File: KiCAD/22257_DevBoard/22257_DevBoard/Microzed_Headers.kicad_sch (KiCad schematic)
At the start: 11 parts, among them J1 TD-120-G-AACON40_2X20_TU_HTS_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, J2 TD-120-G-AACON40_2X20_TU_HTS_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

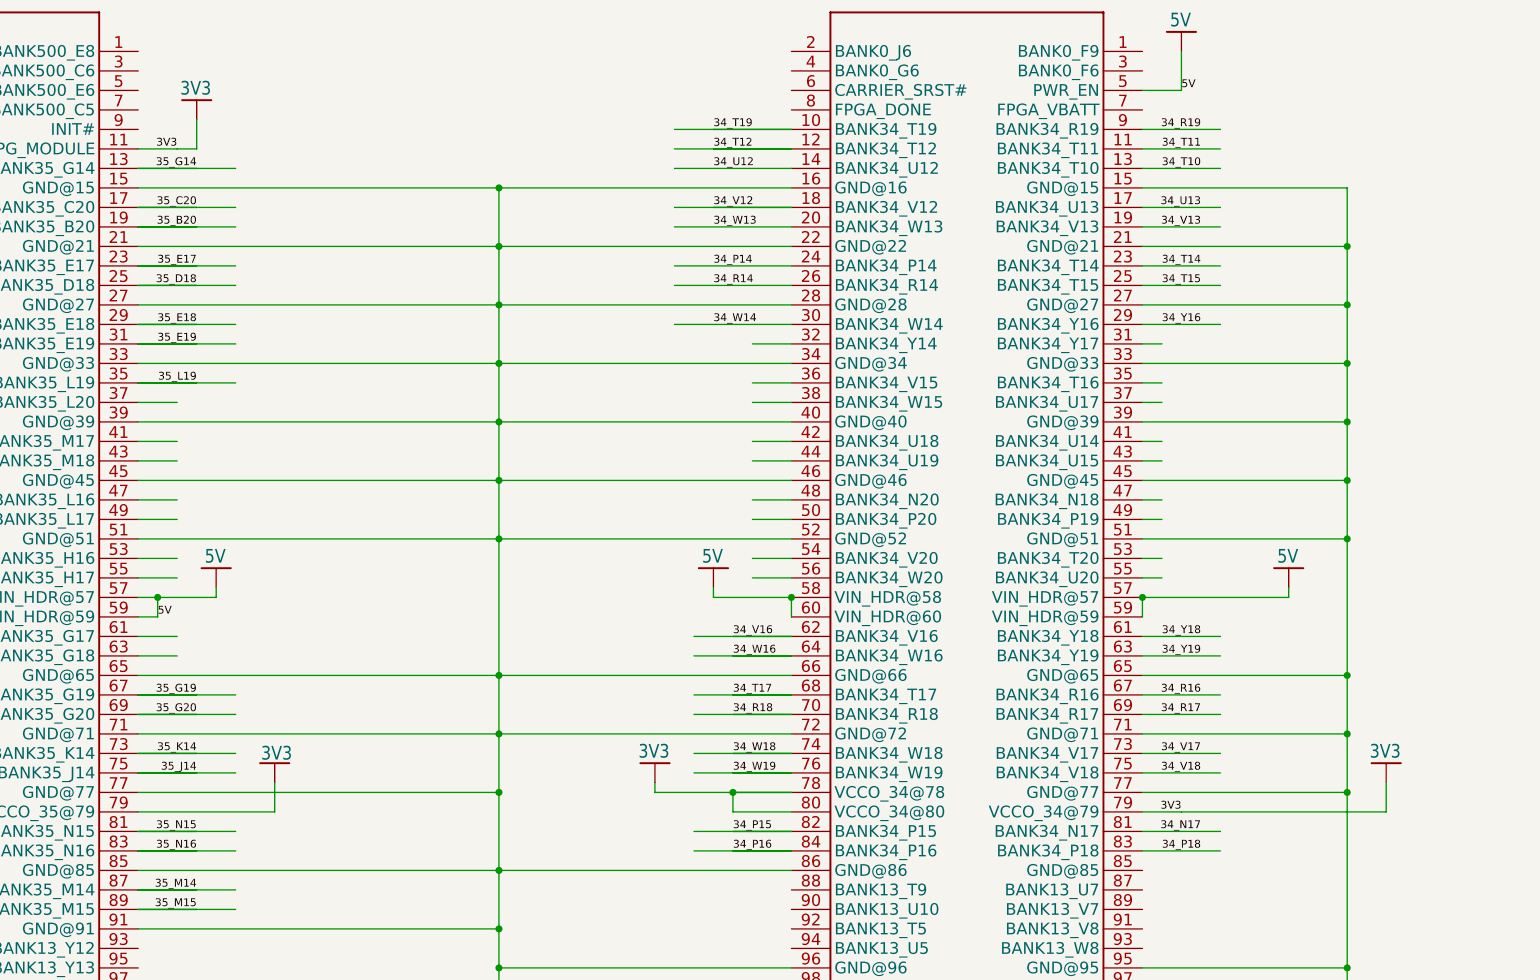
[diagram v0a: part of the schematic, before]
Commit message: Schematic Progress. Added connections to the MicroZed and added a 3v3 rail regulator
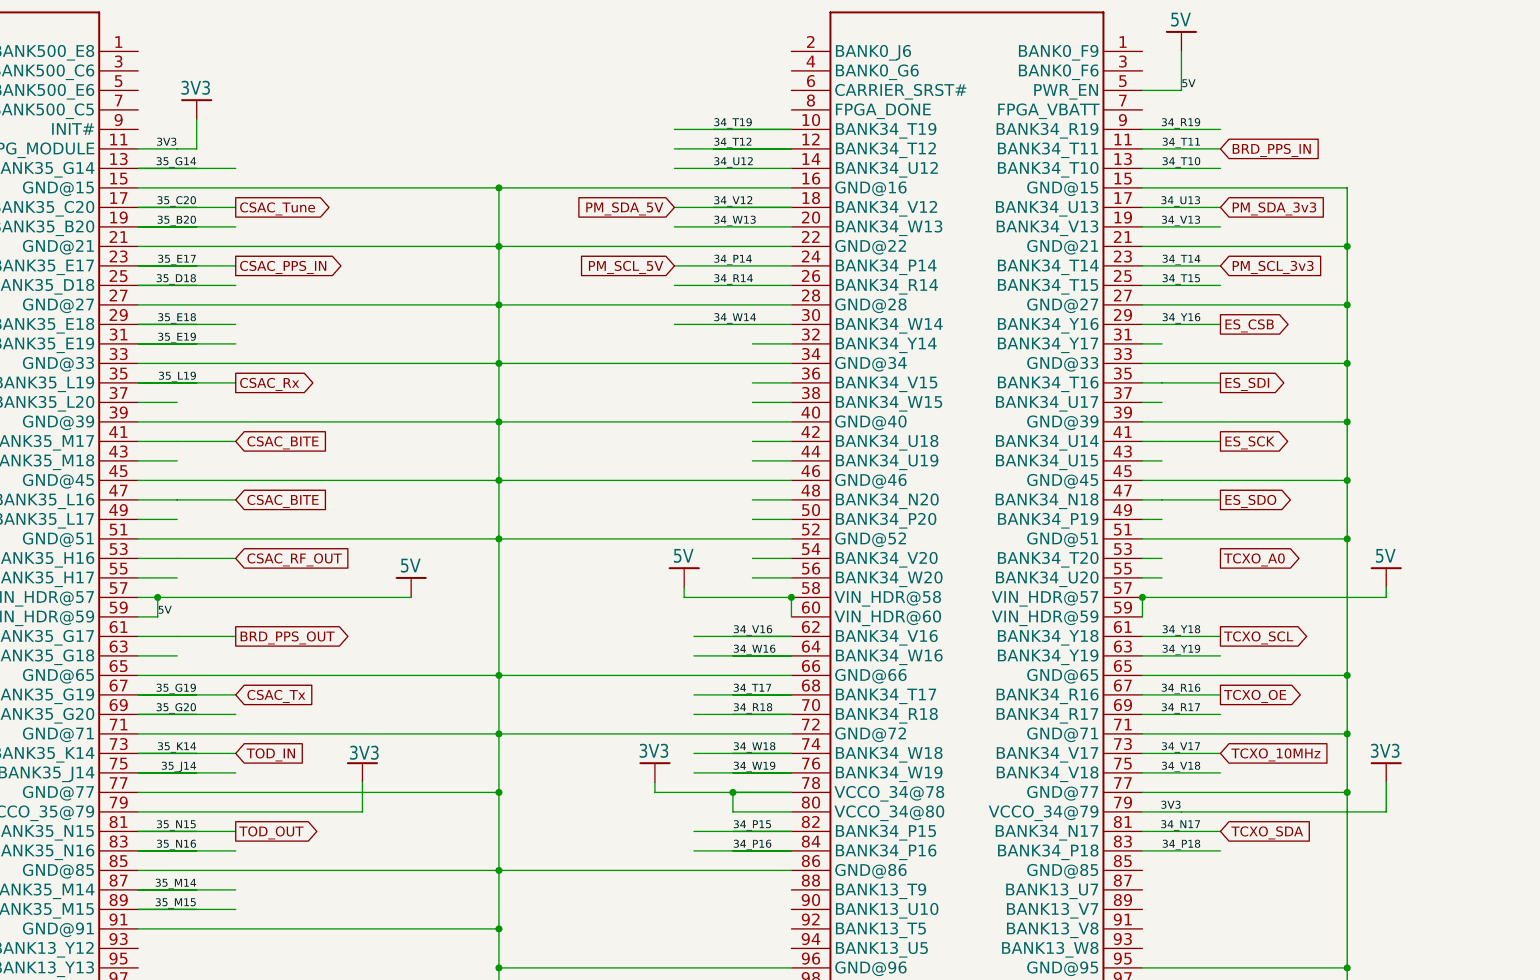
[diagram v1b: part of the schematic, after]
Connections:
- net ES_SDI: now reaches JX2.35 (BANK34_T16)
- net ES_SCK: now reaches JX2.41 (BANK34_U14)
- net ES_SDO: now reaches JX2.47 (BANK34_N18)
- net CSAC_BITE: now reaches JX1.41 (BANK35_M17)
- net CSAC_BITE: now also JX1.47 (BANK35_L16)
- net CSAC_RF_OUT: now reaches JX1.53 (BANK35_H16)
- net BRD_PPS_OUT: now reaches JX1.61 (BANK35_G17)
- net 34_N17 renamed TCXO_SDA
- net 34_P14 renamed PM_SCL_5V
- net 34_R16 renamed TCXO_OE
- net 34_T11 renamed BRD_PPS_IN
- net 34_T14 renamed PM_SCL_3v3
- net 34_U13 renamed PM_SDA_3v3
- net 34_V12 renamed PM_SDA_5V
- net 34_V17 renamed TCXO_10MHz
- net 34_Y16 renamed ES_CSB
- net 34_Y18 renamed TCXO_SCL
- net 35_C20 renamed CSAC_Tune
- net 35_E17 renamed CSAC_PPS_IN
- net 35_G19 renamed CSAC_Tx
- net 35_K14 renamed TOD_IN
- net 35_L19 renamed CSAC_Rx
- net 35_N15 renamed TOD_OUT

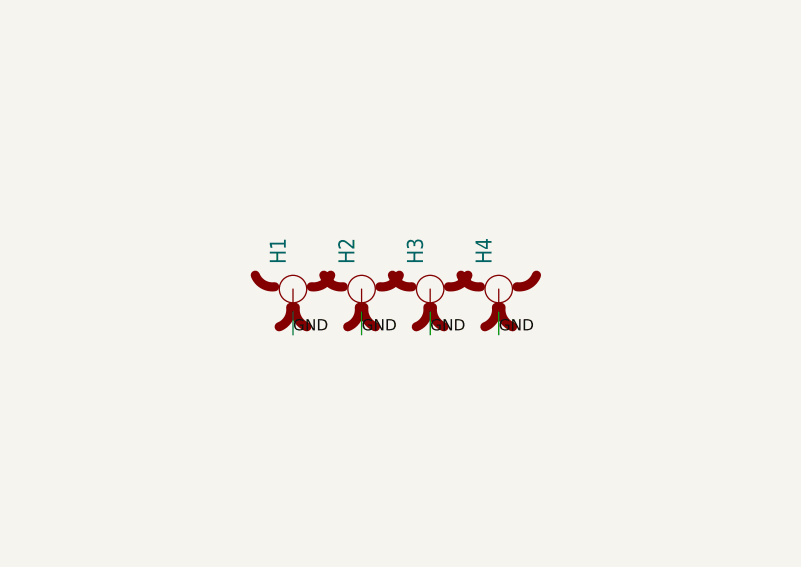
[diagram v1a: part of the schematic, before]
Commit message: More Schematic Updates
Added power monitors and connectors, along with finishing the power circuitry.
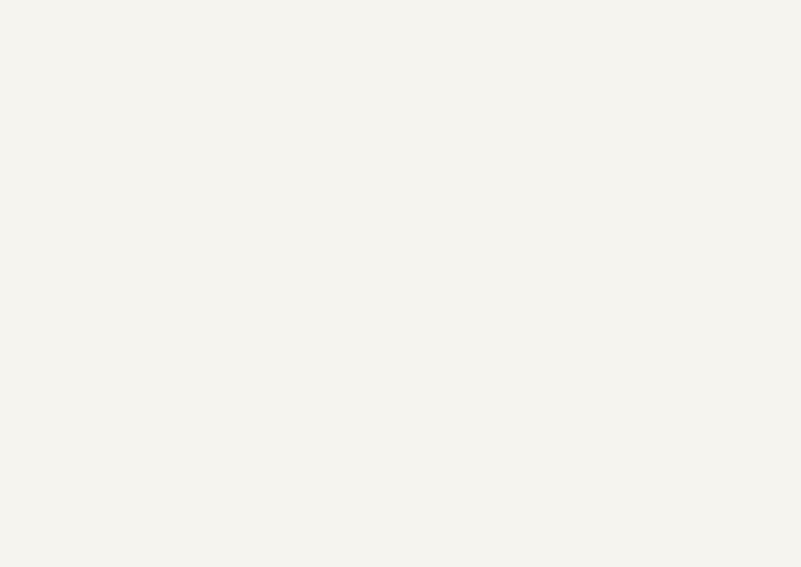
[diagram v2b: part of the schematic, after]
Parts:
- removed H1, H2, H3, H4: MOUNT-PAD-ROUND5.0, ZED_BREAKOUT_v22:5,0-PAD, symbol ZED_BREAKOUT_v22-eagle-import:MOUNT-PAD-ROUND5.0

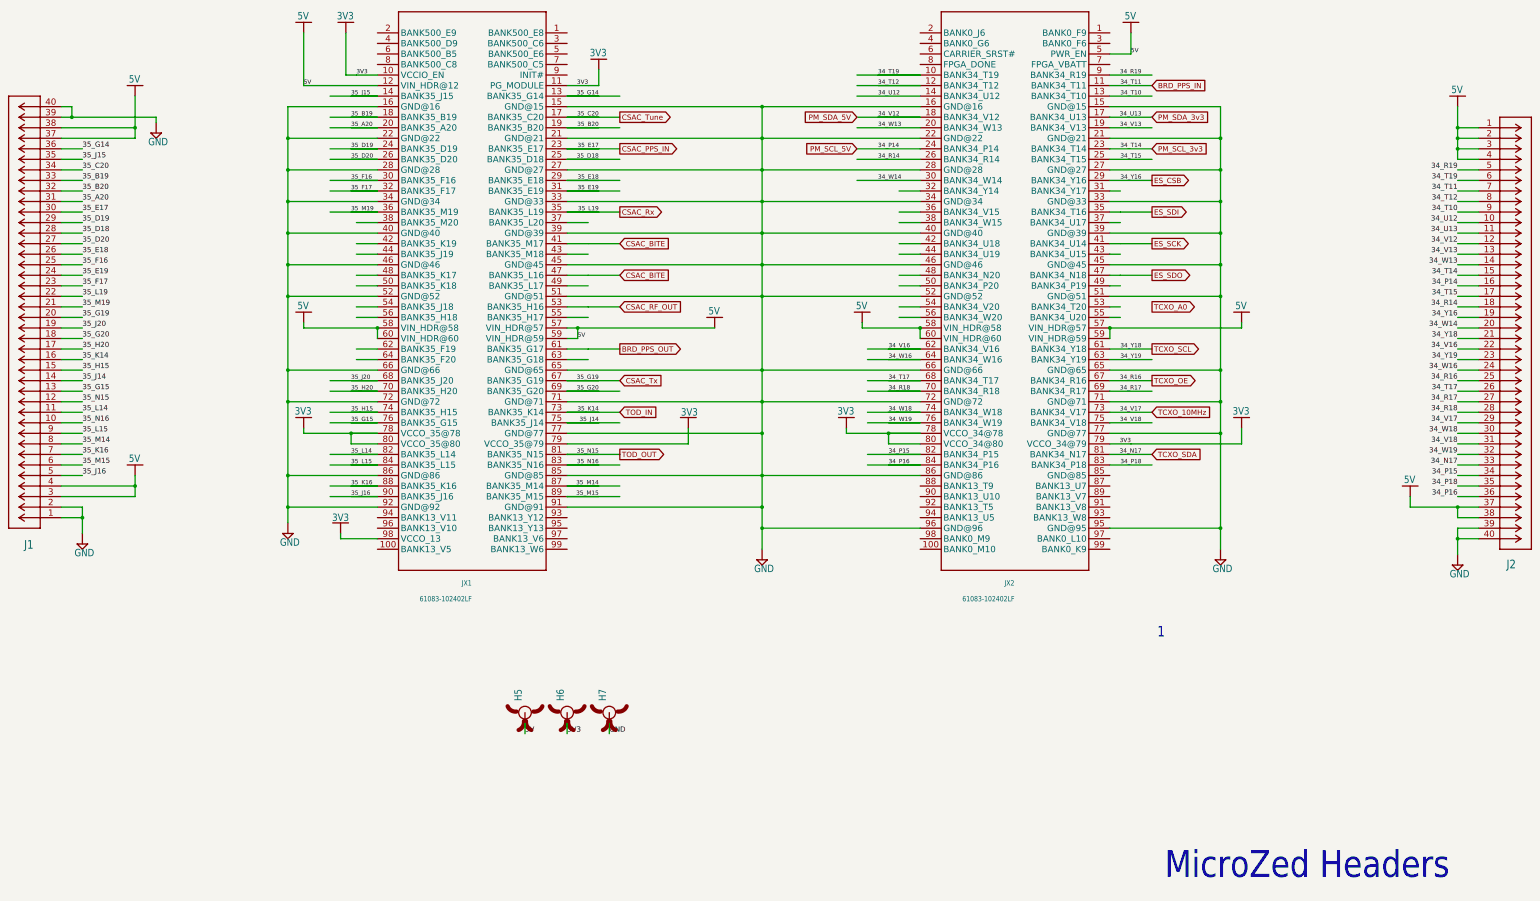
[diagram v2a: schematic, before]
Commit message: Schematic should be finished, onto layout
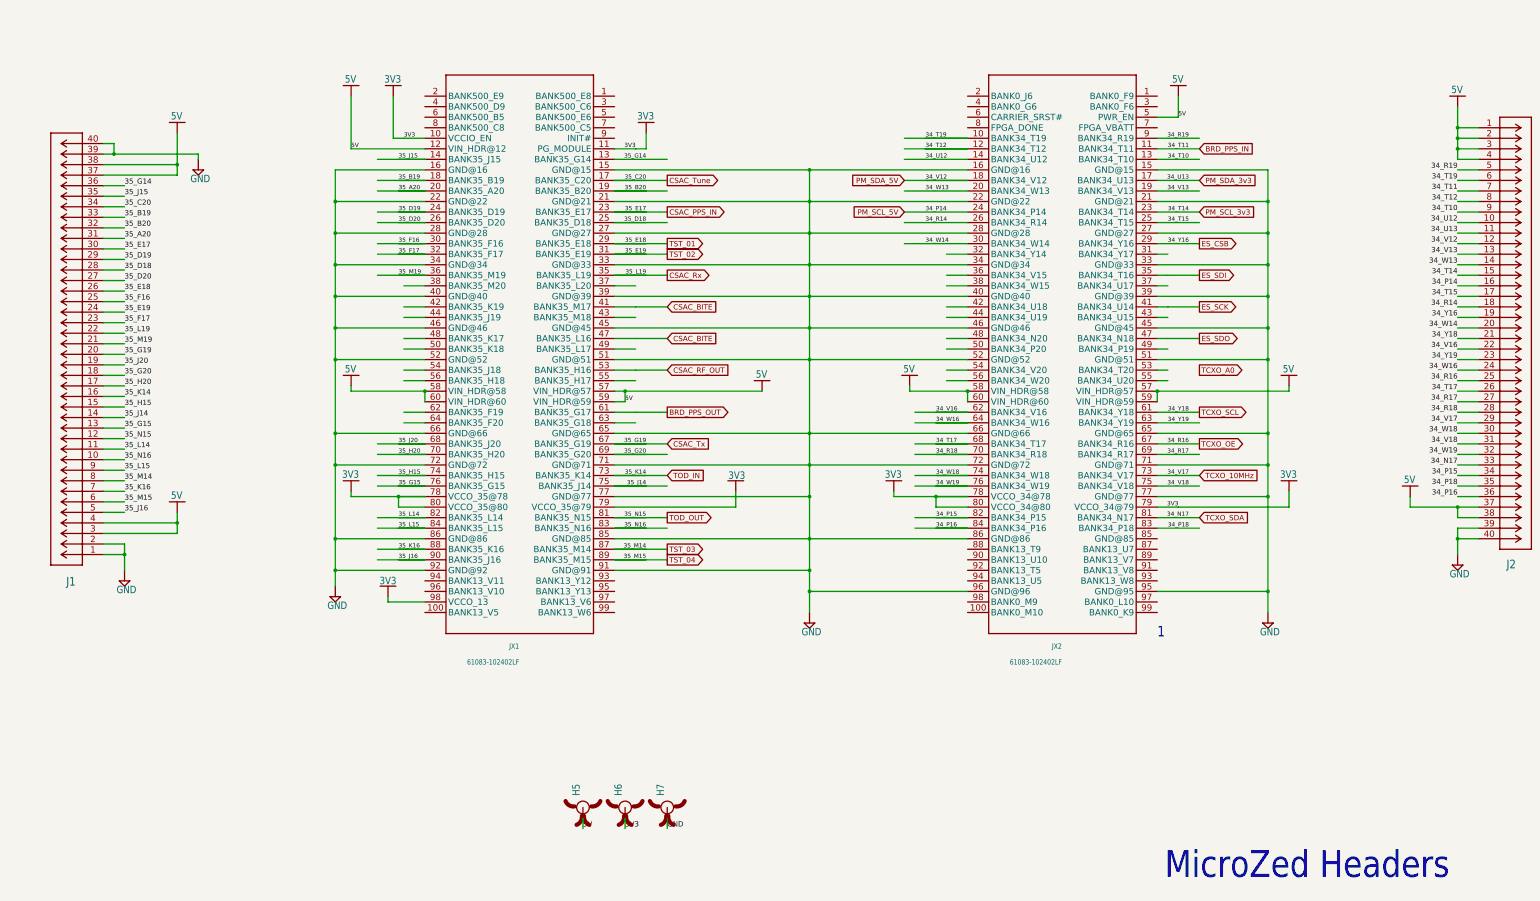
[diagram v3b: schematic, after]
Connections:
- net 35_E18 renamed TST_01
- net 35_E19 renamed TST_02
- net 35_M14 renamed TST_03
- net 35_M15 renamed TST_04
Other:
- moved on the sheet: H5, H6, H7, J1, JX1, JX2

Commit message: Started layout
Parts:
- H5, H6, H7: footprint ZED_BREAKOUT_v22:5,0-PAD -> MountingHole:MountingHole_3.2mm_M3
- J1, J2: footprint ZED_BREAKOUT_v22:CON40_2X20_TU_HTS_SAI -> 22257_DevBoard:CON40_2X20_TU_HTS_SAI
- JX1, JX2: footprint ZED_BREAKOUT_v22:61083-102402LF -> 22257_DevBoard:61083-102402LF_1104291
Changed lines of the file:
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@@
 			)
 		)
-		(property "Footprint" "ZED_BREAKOUT_v22:5,0-PAD"
+		(property "Footprint" "MountingHole:MountingHole_3.2mm_M3"
 			(at 163.83 247.65 0)
 			(effects
@@
 			)
 		)
-		(property "Footprint" "ZED_BREAKOUT_v22:5,0-PAD"
+		(property "Footprint" "MountingHole:MountingHole_3.2mm_M3"
 			(at 184.15 247.65 0)
 			(effects
@@
 			)
 		)
-		(property "Footprint" "ZED_BREAKOUT_v22:61083-102402LF"
+		(property "Footprint" "22257_DevBoard:61083-102402LF_1104291"
 			(at 279.4 137.16 0)
 			(effects
@@
 			)
 		)
-		(property "Footprint" "ZED_BREAKOUT_v22:5,0-PAD"
+		(property "Footprint" "MountingHole:MountingHole_3.2mm_M3"
 			(at 173.99 247.65 0)
 			(effects
@@
 			)
 		)
-		(property "Footprint" "ZED_BREAKOUT_v22:61083-102402LF"
+		(property "Footprint" "22257_DevBoard:61083-102402LF_1104291"
 			(at 148.59 137.16 0)
 			(effects
@@
 			)
 		)
-		(property "Footprint" "ZED_BREAKOUT_v22:CON40_2X20_TU_HTS_SAI"
+		(property "Footprint" "22257_DevBoard:CON40_2X20_TU_HTS_SAI"
 			(at 379.73 83.82 0)
 			(effects
@@
 			)
 		)
-		(property "Footprint" "ZED_BREAKOUT_v22:CON40_2X20_TU_HTS_SAI"
+		(property "Footprint" "22257_DevBoard:CON40_2X20_TU_HTS_SAI"
 			(at 48.26 186.69 0)
 			(effects

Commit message: Finished Component Placement and Arrangement.
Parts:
- removed H5, H6, H7: MOUNT-PAD-ROUND5.0, MountingHole:MountingHole_3.2mm_M3, symbol ZED_BREAKOUT_v22-eagle-import:MOUNT-PAD-ROUND5.0

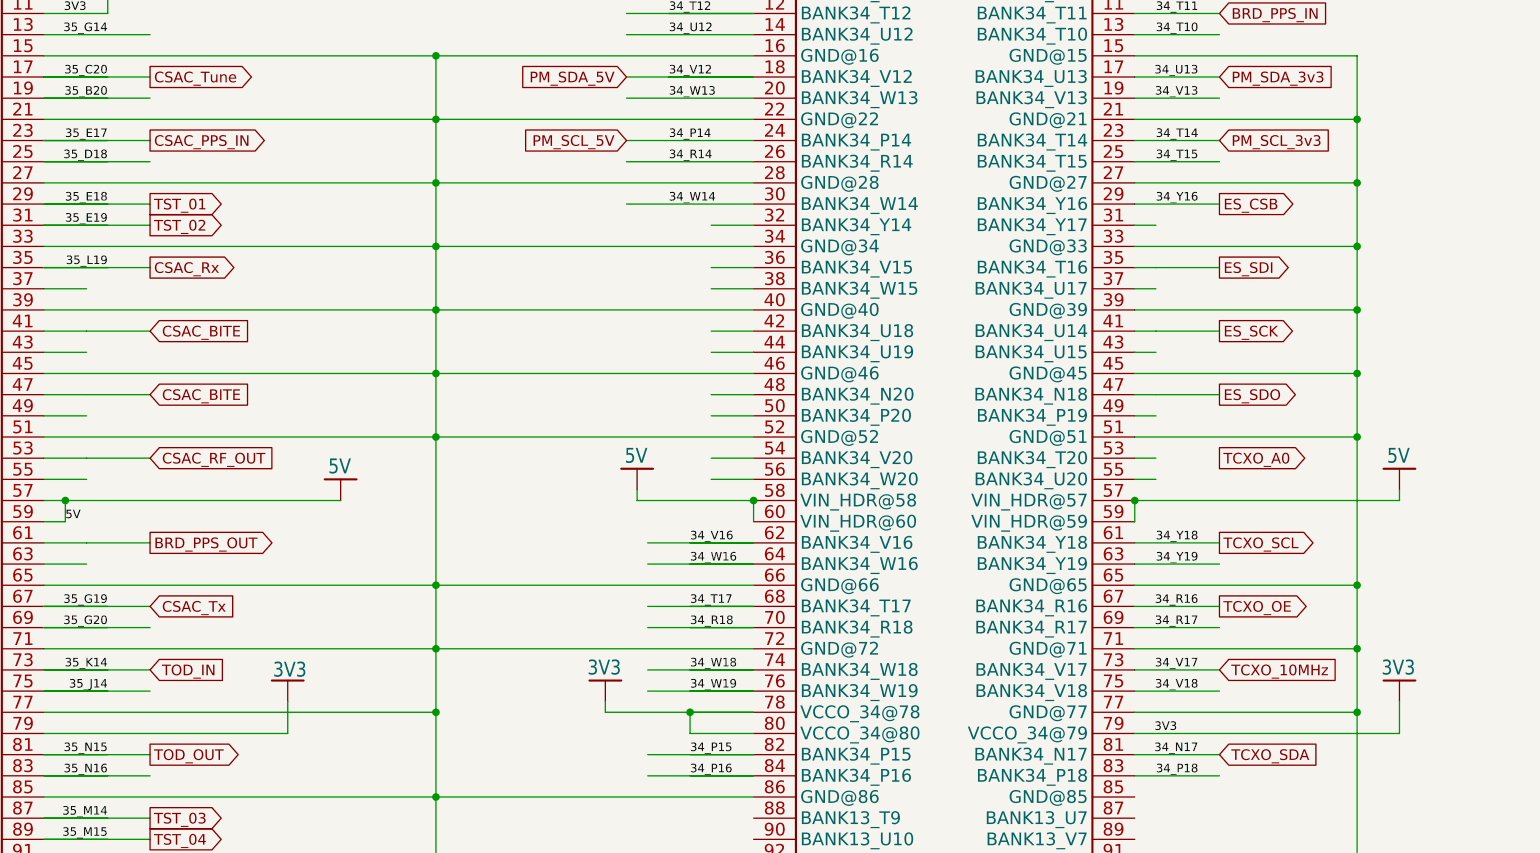
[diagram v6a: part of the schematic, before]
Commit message: A lot of routing progress done
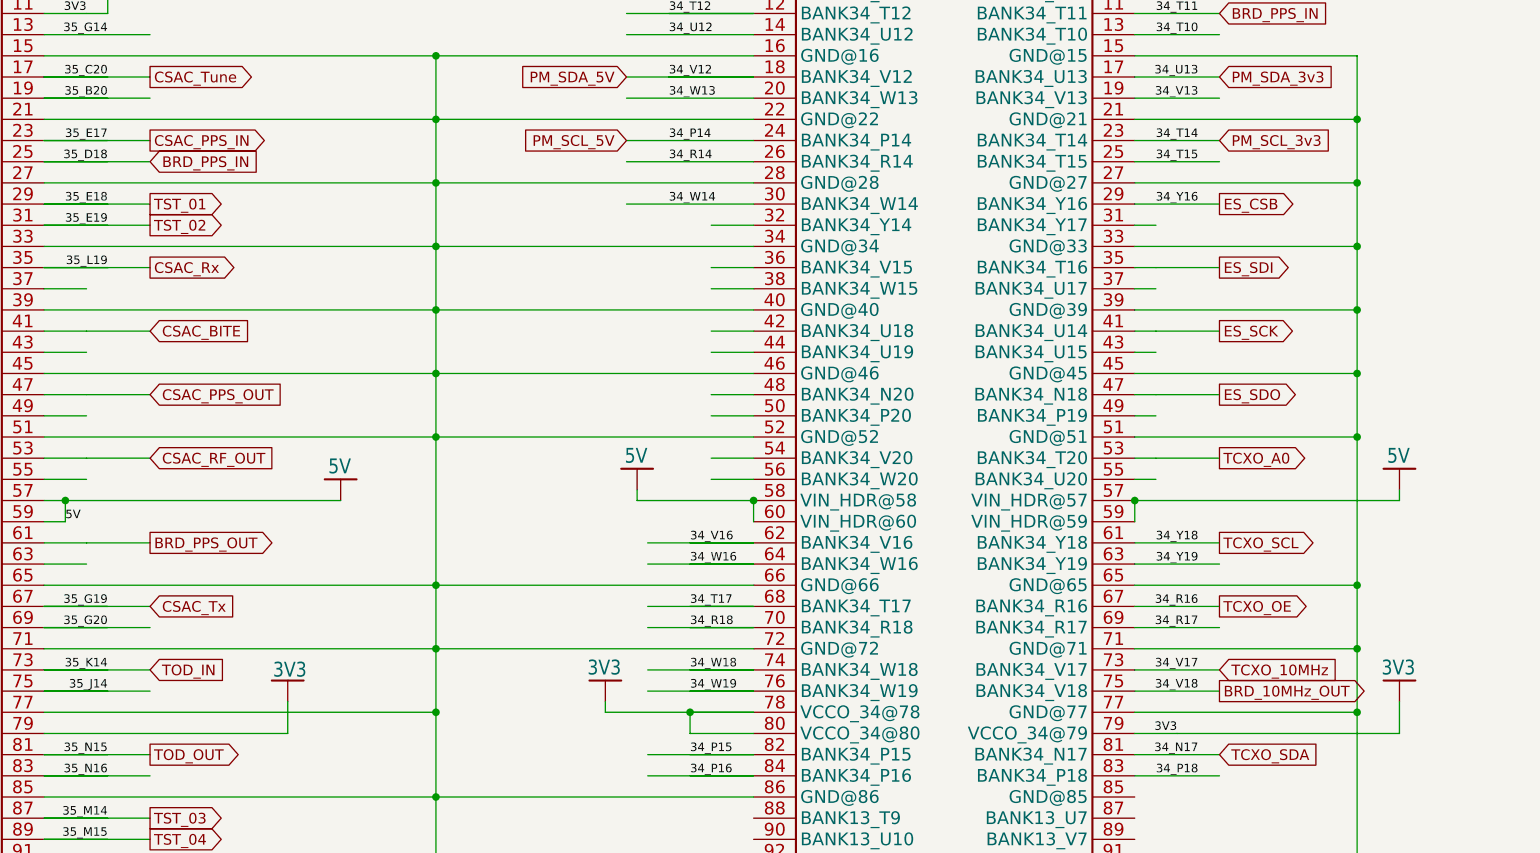
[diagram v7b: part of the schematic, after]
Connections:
- net 35_D18 is gone; now on net BRD_PPS_IN: J1.28, JX1.25 (BANK35_D18)
- net CSAC_BITE: no longer JX1.47 (BANK35_L16)
- net TCXO_A0: now also JX2.53 (BANK34_T20)
- net 34_V18 renamed BRD_10MHz_OUT
- new net CSAC_PPS_OUT: JX1.47 (BANK35_L16)
